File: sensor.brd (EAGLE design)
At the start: 30.5 x 35.6 mm, 17 parts, among them IC1 TINY261A

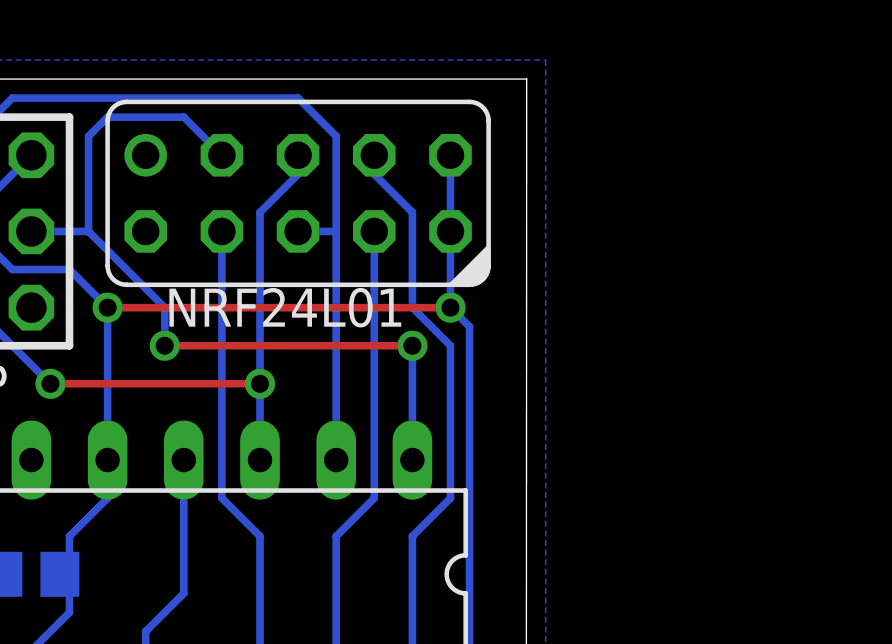
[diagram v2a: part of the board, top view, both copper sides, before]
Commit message: series resistors for shared spi/isp interface
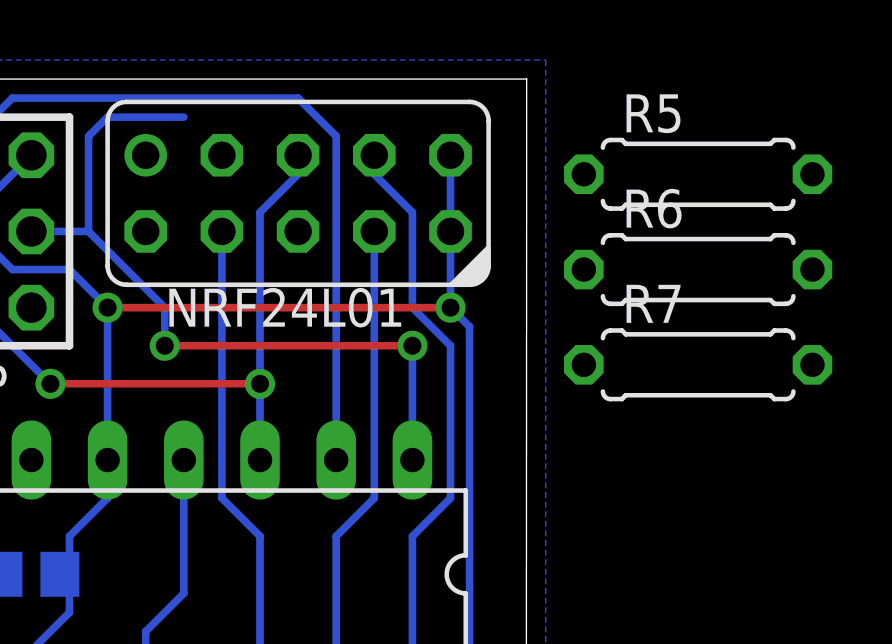
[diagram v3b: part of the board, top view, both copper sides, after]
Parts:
- added R5, R6, R7: 4k7, rcl:0207/7
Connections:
- new net N$3: NRF24L01.5, R5.2
- new net N$4: NRF24L01.3, R6.2
- new net N$5: NRF24L01.6, R7.1
- net PB0: now also R6.1; no longer NRF24L01.3
- net PB1: now also R7.2; no longer NRF24L01.6
- net PB2: now also R5.1; no longer NRF24L01.5
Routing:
- net PB0: track 27.2 -> 25.4 mm
- net PB1: track 26.1 -> 24.8 mm
- net PB2: track 24.1 -> 23.4 mm
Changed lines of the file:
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@@
 <layer number="21" name="tPlace" color="7" fill="1" visible="yes" active="yes"/>
 <layer number="22" name="bPlace" color="7" fill="1" visible="yes" active="yes"/>
-<layer number="23" name="tOrigins" color="15" fill="1" visible="no" active="yes"/>
+<layer number="23" name="tOrigins" color="15" fill="1" visible="yes" active="yes"/>
 <layer number="24" name="bOrigins" color="15" fill="1" visible="yes" active="yes"/>
 <layer number="25" name="tNames" color="7" fill="1" visible="yes" active="yes"/>
@@
 <attribute name="VALUE" x="0" y="31.75" size="1.27" layer="27" rot="R270"/>
 </element>
+<element name="R5" library="rcl" package="0207/7" value="4k7" x="36.195" y="32.385"/>
+<element name="R6" library="rcl" package="0207/7" value="4k7" x="36.195" y="29.21"/>
+<element name="R7" library="rcl" package="0207/7" value="4k7" x="36.195" y="26.035"/>
 </elements>
 <signals>
@@
 <wire x1="18.415" y1="26.67" x2="26.67" y2="26.67" width="0.254" layer="1"/>
 <via x="26.67" y="26.67" extent="1-16" drill="0.6"/>
-<contactref element="NRF24L01" pad="3"/>
-<wire x1="20.32" y1="33.02" x2="19.05" y2="34.29" width="0.254" layer="16"/>
 <wire x1="19.05" y1="34.29" x2="16.51" y2="34.29" width="0.254" layer="16"/>
 <wire x1="16.51" y1="34.29" x2="15.875" y2="33.655" width="0.254" layer="16"/>
 <wire x1="15.875" y1="33.655" x2="15.875" y2="30.48" width="0.254" layer="16"/>
 <wire x1="15.875" y1="30.48" x2="13.97" y2="30.48" width="0.254" layer="16"/>
+<contactref element="R6" pad="1"/>
+<wire x1="32.385" y1="29.21" x2="18.415" y2="26.67" width="0" layer="19" extent="1-1"/>
 </signal>
 <signal name="PB1">
 <contactref element="ISP" pad="1"/>
 <contactref element="IC1" pad="2"/>
-<wire x1="24.13" y1="22.86" x2="24.13" y2="30.48" width="0.254" layer="16"/>
-<contactref element="NRF24L01" pad="6"/>
-<wire x1="22.86" y1="30.48" x2="24.13" y2="30.48" width="0.254" layer="16"/>
-<wire x1="24.13" y1="30.48" x2="24.13" y2="33.655" width="0.254" layer="16"/>
+<wire x1="24.13" y1="22.86" x2="24.13" y2="33.655" width="0.254" layer="16"/>
 <wire x1="24.13" y1="33.655" x2="22.86" y2="34.925" width="0.254" layer="16"/>
 <wire x1="22.86" y1="34.925" x2="13.335" y2="34.925" width="0.254" layer="16"/>
 <wire x1="13.335" y1="34.925" x2="11.43" y2="33.02" width="0.254" layer="16"/>
+<contactref element="R7" pad="2"/>
+<wire x1="40.005" y1="26.035" x2="24.13" y2="22.86" width="0" layer="19" extent="1-1"/>
 </signal>
 <signal name="PB2">
-<contactref element="NRF24L01" pad="5"/>
 <contactref element="ISP" pad="3"/>
 <contactref element="IC1" pad="3"/>
-<wire x1="22.86" y1="33.02" x2="22.86" y2="32.385" width="0.254" layer="16"/>
 <wire x1="22.86" y1="32.385" x2="21.59" y2="31.115" width="0.254" layer="16"/>
 <wire x1="21.59" y1="31.115" x2="21.59" y2="25.4" width="0.254" layer="16"/>
@@
 <wire x1="14.605" y1="25.4" x2="21.59" y2="25.4" width="0.254" layer="1"/>
 <via x="21.59" y="25.4" extent="1-16" drill="0.6"/>
+<contactref element="R5" pad="1"/>
+<wire x1="32.385" y1="32.385" x2="14.605" y2="25.4" width="0" layer="19" extent="16-16"/>
 </signal>
 <signal name="PB3">
@@
 <wire x1="18.73" y1="9.84" x2="17.61" y2="9.84" width="0.254" layer="16"/>
 </signal>
+<signal name="N$3">
+<contactref element="NRF24L01" pad="5"/>
+<contactref element="R5" pad="2"/>
+<wire x1="40.005" y1="32.385" x2="22.86" y2="33.02" width="0" layer="19" extent="1-1"/>
+</signal>
+<signal name="N$4">
+<contactref element="R6" pad="2"/>
+<contactref element="NRF24L01" pad="3"/>
+<wire x1="40.005" y1="29.21" x2="20.32" y2="33.02" width="0" layer="19" extent="1-1"/>
+</signal>
+<signal name="N$5">
+<contactref element="NRF24L01" pad="6"/>
+<contactref element="R7" pad="1"/>
+<wire x1="32.385" y1="26.035" x2="22.86" y2="30.48" width="0" layer="19" extent="1-1"/>
+</signal>
 </signals>
